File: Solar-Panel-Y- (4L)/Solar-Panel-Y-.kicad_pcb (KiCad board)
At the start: 4 copper layers, 64 x 58 mm, 85 parts, among them J1 FTS-105-01-L-DV-A, J2 BM02B-SRSS-TB, Q1 BSS138DWQ-7, Q2 MBT2222ADW1T1, Q3 BSS138DWQ-7, Q4 MBT2222ADW1T1, SW1 D2F-L2-A1, SW2 D2F-L2-A, U1 BQ25570RGRR, U2 TSL2561

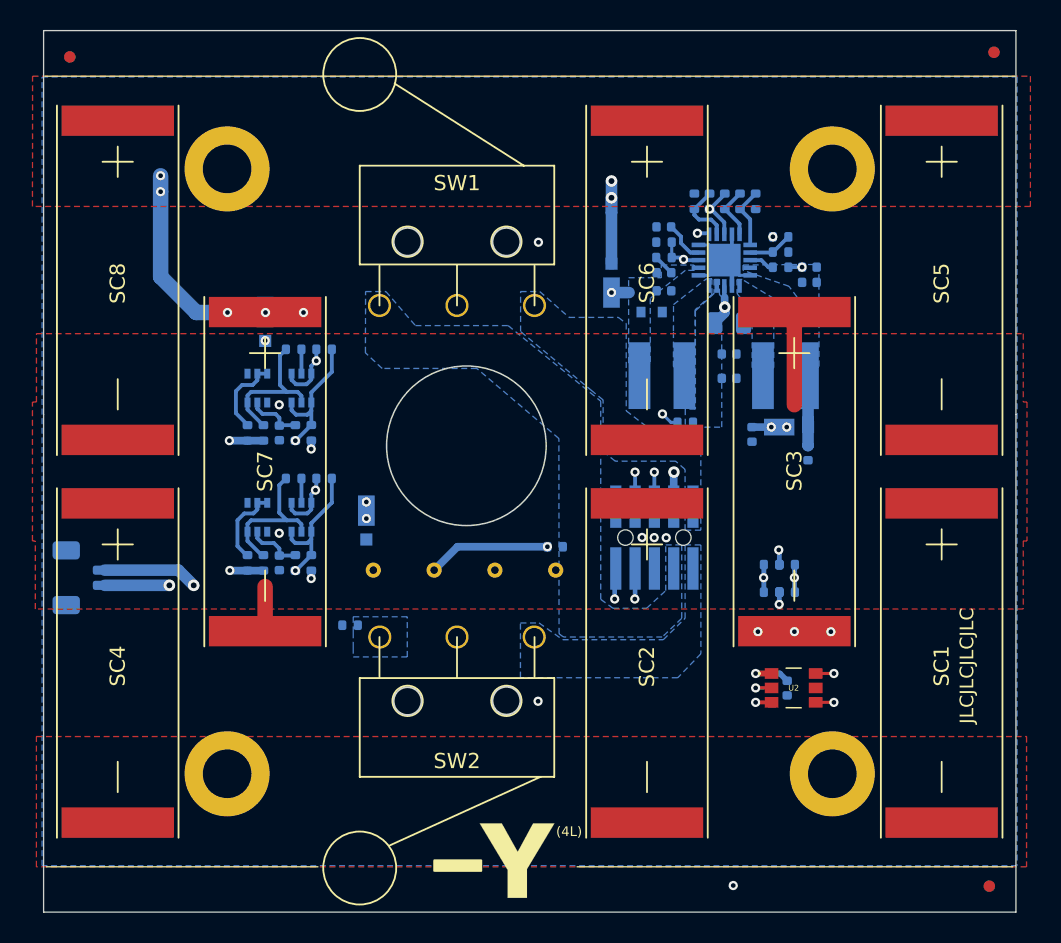
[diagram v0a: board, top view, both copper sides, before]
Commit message: Updated all solar panels to Rev B2/01 + Export STEP / BOM
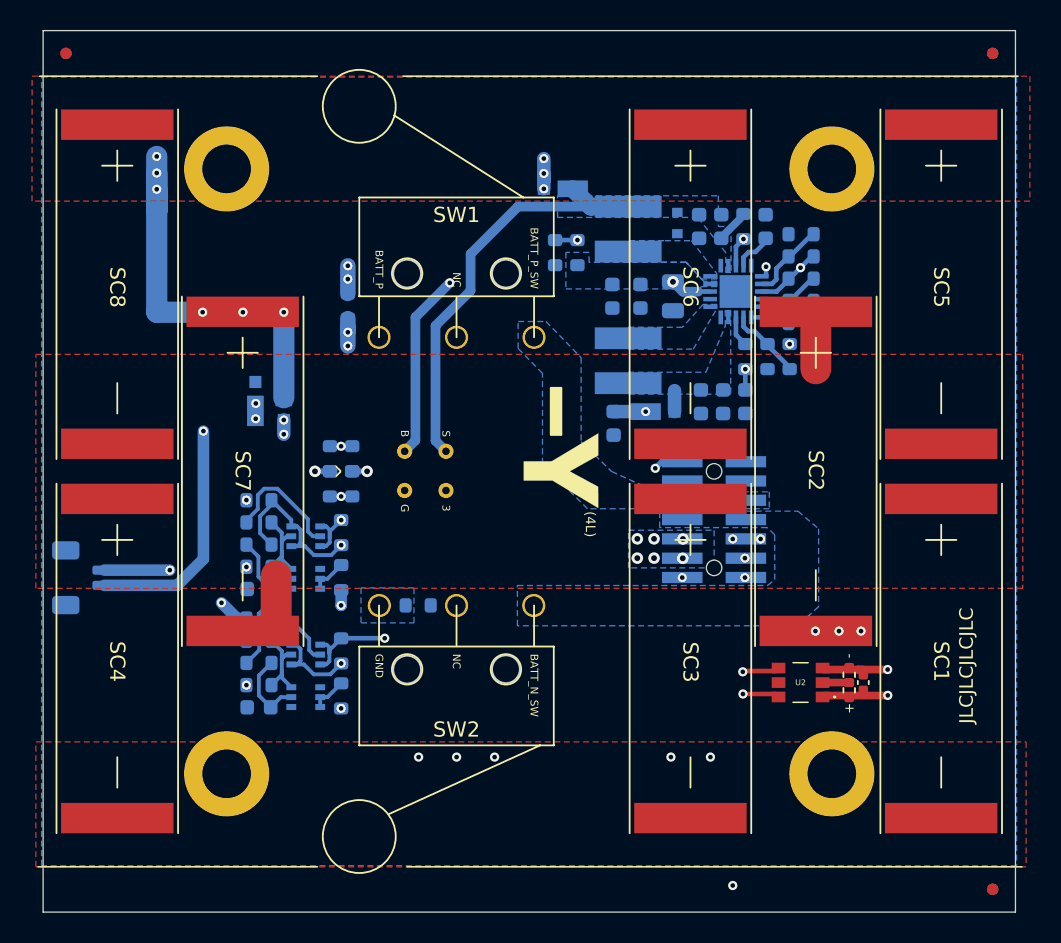
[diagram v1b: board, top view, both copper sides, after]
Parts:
- removed the Ref** at (96.5, 83.8)
- removed TP1, TP2, TP3, TP4: TP, TestPoint:TestPoint_THTPad_D1.0mm_Drill0.5mm
- added 3: TP, TestPoint:TestPoint_THTPad_D1.0mm_Drill0.5mm, B.Cu at (99.6, 65.3)
- added B: TP, TestPoint:TestPoint_THTPad_D1.0mm_Drill0.5mm, B.Cu at (96.9, 62.7)
- added G: TP, TestPoint:TestPoint_THTPad_D1.0mm_Drill0.5mm, B.Cu at (96.9, 65.3)
- added Ref**: Val**, custom-footprints:pycubed_mini_half, B.Cu at (104.6, 85.6)
- added S: TP, TestPoint:TestPoint_THTPad_D1.0mm_Drill0.5mm, B.Cu at (99.6, 62.7)
- C1, R1, R2: moved to F.Cu
- C10, C11, C12, C13, C2, C3, C4, C6, C7, C8, C9: footprint Capacitor_SMD:C_0402_1005Metric -> Capacitor_SMD:C_0603_1608Metric
- J1: value FTS-105-01-L-DV-A -> FTS-107-01-X-DV-A; footprint batteryboard:FTS-105-XX-YY-DV-A -> batteryboard:SAMTEC-FTS-107-01-X-DV-A
- R10, R11, R12, R13, R16, R17, R18, R3, R5, R6, R7, R8, R9: footprint Resistor_SMD:R_0402_1005Metric -> Resistor_SMD:R_0603_1608Metric
- R14, R15: value 0 -> DNI; footprint Resistor_SMD:R_0402_1005Metric -> Resistor_SMD:R_0603_1608Metric
- R19: renamed from R22; value 0 -> DNI; footprint Resistor_SMD:R_0402_1005Metric -> Resistor_SMD:R_0603_1608Metric
- R20: renamed from R23; value 0 -> DNI; footprint Resistor_SMD:R_0402_1005Metric -> Resistor_SMD:R_0603_1608Metric
- R21: renamed from R4; footprint Resistor_SMD:R_0402_1005Metric -> Resistor_SMD:R_0603_1608Metric
- R22: renamed from R21; footprint Resistor_SMD:R_0402_1005Metric -> Resistor_SMD:R_0603_1608Metric
- R23: renamed from R24; footprint Resistor_SMD:R_0402_1005Metric -> Resistor_SMD:R_0603_1608Metric
- R24: renamed from R25; footprint Resistor_SMD:R_0402_1005Metric -> Resistor_SMD:R_0603_1608Metric
- R25: renamed from R26; footprint Resistor_SMD:R_0402_1005Metric -> Resistor_SMD:R_0603_1608Metric
- R26: renamed from R27; footprint Resistor_SMD:R_0402_1005Metric -> Resistor_SMD:R_0603_1608Metric
- R27: renamed from R28; footprint Resistor_SMD:R_0402_1005Metric -> Resistor_SMD:R_0603_1608Metric
- R28: renamed from R29; footprint Resistor_SMD:R_0402_1005Metric -> Resistor_SMD:R_0603_1608Metric
- R29: renamed from R30; footprint Resistor_SMD:R_0402_1005Metric -> Resistor_SMD:R_0603_1608Metric
- R30: renamed from R31; footprint Resistor_SMD:R_0402_1005Metric -> Resistor_SMD:R_0603_1608Metric
- R31: renamed from R20; footprint Resistor_SMD:R_0402_1005Metric -> Resistor_SMD:R_0603_1608Metric
- R4: renamed from R19; footprint Resistor_SMD:R_0402_1005Metric -> Resistor_SMD:R_0603_1608Metric
- moved R12 30.9 mm to (92.0, 63.2), turned to 90 degrees
- moved R17 29.9 mm to (93.4, 63.2), turned to 90 degrees
- moved R13 29.5 mm to (92.0, 64.8), turned to 90 degrees
- moved R18 28.5 mm to (93.4, 64.8), turned to 90 degrees
- moved R3 20.9 mm to (93.1, 53.1), turned to 90 degrees
- moved Ref** 17.8 mm to (106.2, 81.0), turned to -90 degrees
- moved R16 13.2 mm to (108.2, 49.6), turned to 90 degrees
- moved Q1 12.9 mm to (90.4, 71.1), turned to 180 degrees
- moved Q3 12.3 mm to (90.4, 78.9), turned to 180 degrees
- moved R19 12.1 mm to (92.7, 68.0), turned to 90 degrees
- moved R21 11.6 mm to (87.3, 67.4), turned to 0 degrees
- moved R20 11.4 mm to (92.7, 75.8), turned to 90 degrees
- moved R22 11.3 mm to (92.7, 71.0)
- moved R26 10.9 mm to (87.3, 75.1), turned to 0 degrees
- moved D3 10.7 mm to (87.1, 59.4), turned to 90 degrees
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- renumbered SC3 to SC2, SC2 to SC3
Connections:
- J1 pad 1: BATT_N_SW -> unconnected-(J1-Pad1)
- J1 pad 10: VUSB -> BATT_P
- J1 pad 2: BATT_P_SW -> COIL_P
- J1 pad 3: BATT_P -> GND
- J1 pad 4: +3V3 -> GND
- J1 pad 5: GND -> BATT_P_SW
- J1 pad 6: SCL3 -> BATT_P_SW
- J1 pad 7: COIL_P -> BATT_N_SW
- J1 pad 8: SDA3 -> BATT_N_SW
- J1 pad 9: COIL_N -> +3V3
- Q2 pad 1: SCL3 -> SCL
- Q2 pad 3: SCL3 -> SCL
- Q4 pad 1: SDA3 -> SDA
- Q4 pad 3: SDA3 -> SDA
- R19 pad 2: SCL3 -> SCL
- R20 pad 2: SDA3 -> SDA
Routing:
- net /coil: track 7283.3 -> 7479.5 mm
- net SDA3: track 37.5 -> 0.00 mm, vias 2 -> 0
- net SDA: track 0.00 -> 35.1 mm, vias 0 -> 2
- net SCL3: track 33.8 -> 0.00 mm, vias 2 -> 0
- net SCL: track 0.00 -> 32.7 mm, vias 0 -> 2
- net VBAT: track 35.6 -> 16.8 mm, vias 2 -> 4
- net COIL_P: track 14.6 -> 32.4 mm
- net SCL_LS: track 60.8 -> 49.6 mm
- net COIL_N: track 17.4 -> 26.6 mm
- net VSOLAR: track 24.0 -> 32.1 mm, vias 1 -> 0
- net /VSOLAR_FULL: track 23.5 -> 30.6 mm, vias 7 -> 9
- net Net-(Q2-Pad2): track 1.60 -> 8.03 mm
- net Net-(Q4-Pad2): track 1.60 -> 7.80 mm
- net SDA_LS: track 49.0 -> 43.2 mm
- net GND: track 9.43 -> 4.56 mm, vias 11 -> 9
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- added copper zone on In2.Cu, net +3V3
- added copper zone on In1.Cu, net BATT_P
- added copper zone on In1.Cu, net VBAT
- removed copper zone on In1.Cu, net +3V3
- removed copper zone on In2.Cu, net GND
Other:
- outline, holes or cut-outs redrawn
- board text added: "1.NC 3.GND 5.BATT_P_SW 7.BATT_N_SW 9.3V3 11.SDA 13.SCL"
- board text added: "2.COIL_P 4.GND 6.BATT_P_SW 8.BATT_N_SW 10.BATT_P 12.BATT_P 14.COIL_N"
- board text added: "BATT_N_SW"
- board text added: "BATT_P"
- board text added: "BATT_P_SW"
- board text added: "NC"
- board text added: "Rev B2/01"
- board text added: "^"
- board text added: "⊗"
- board text added: "⊙"
- board text removed: "1.BATT_N_SW 3.BATT_P 5.GND 7.COIL_P 9.COIL_N"
- board text removed: "2.BATT_P_SW 4.3V3 6.SCL3 8.SDA3 10.VUSB"
- board text removed: "Rev B1/02"

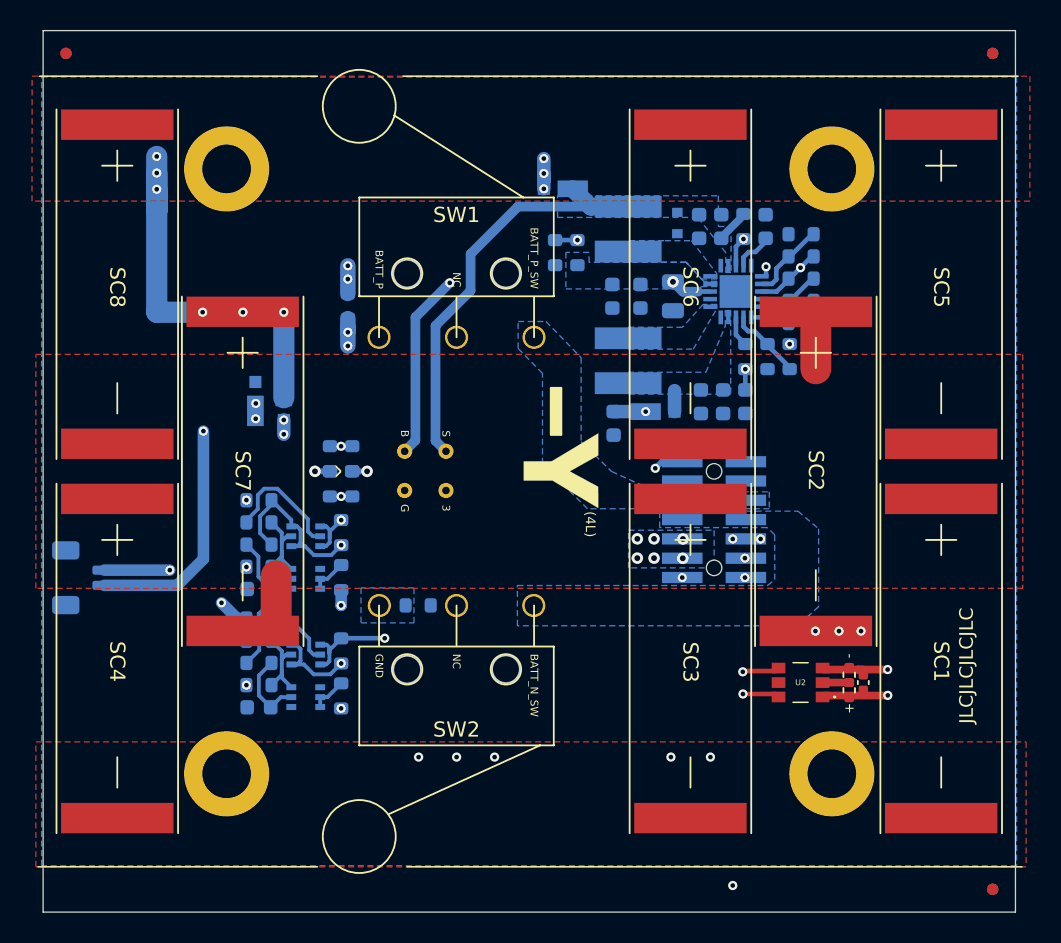
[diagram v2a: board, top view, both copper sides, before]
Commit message: Fix Rail Interference issues
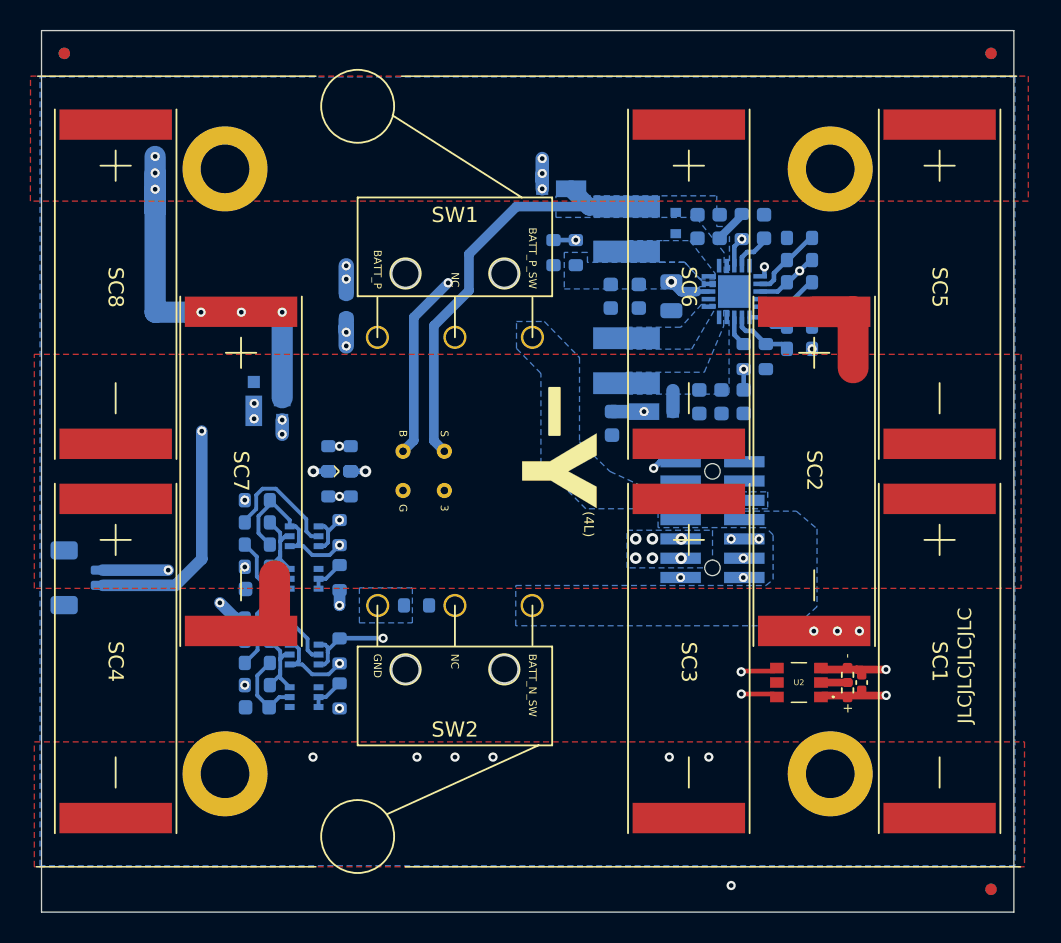
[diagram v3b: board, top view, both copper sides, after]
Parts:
- moved R10 0.82 mm to (122.9, 55.9), turned to 0 degrees
- moved R5 0.26 mm to (122.9, 50.1)
- moved R6 0.26 mm to (122.9, 48.6)
- moved R7 0.26 mm to (122.9, 51.6)
- moved R8 0.26 mm to (122.9, 53.0)
- moved R9 0.26 mm to (122.9, 54.5)
- moved Q4 0.11 mm to (90.3, 76.1)
- moved SC1 0.11 mm to (132.1, 65.8)
- moved SC3 0.11 mm to (115.6, 65.8)
- moved SC4 0.11 mm to (77.9, 65.8)
- moved C8 0.11 mm to (117.7, 59.4)
- moved L1 0.11 mm to (111.5, 48.1)
- moved C1 0.11 mm to (127.0, 77.9)
- moved C12 0.11 mm to (87.2, 71.7)
- moved C13 0.11 mm to (87.2, 79.5)
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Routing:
- net Net-(D3-Pad1): track 8.33 -> 10.8 mm
- net Net-(R10-Pad1): track 4.72 -> 4.20 mm
- net GND: vias 9 -> 10
